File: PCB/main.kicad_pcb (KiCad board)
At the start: 2 copper layers, 21 parts, among them SW1 SPST, U1 MCP2558FD, U2 MCP2558FD, U3 STM32G0B1, Y1 40M

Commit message: Further develop board
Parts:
- added C10: 100u, Capacitor_Tantalum_SMD:CP_EIA-3528-15_AVX-H, F.Cu at (37.7, 48.5)
- added C11: 1u, Capacitor_SMD:C_0805_2012Metric, F.Cu at (32.5, 46.5)
- added C12: 1u, Capacitor_SMD:C_0805_2012Metric, F.Cu at (32.5, 49.5)
- added C13: 100n, Capacitor_SMD:C_0402_1005Metric, F.Cu at (45.7, 37.0)
- added C14: 100n, Capacitor_SMD:C_0402_1005Metric, F.Cu at (45.7, 39.0)
- added C15: 100n, Capacitor_SMD:C_0402_1005Metric, F.Cu at (45.7, 41.0)
- added C7: 100n, Capacitor_SMD:C_0603_1608Metric, F.Cu at (14.7, 48.8)
- added C8: 330u, Capacitor_SMD:CP_Elec_10x10, F.Cu at (37.5, 36.1)
- added C9: 100u, Capacitor_Tantalum_SMD:CP_EIA-3528-15_AVX-H, F.Cu at (37.7, 44.2)
- added D1: SS36, Diode_SMD:D_SMC, F.Cu at (7.28, 46.4)
- added J1: S20B-PADSS-1, libdb:CMP-0012, F.Cu at (15.0, 8.51)
- added J2: S20B-PADSS-1, libdb:CMP-0012, F.Cu at (30.3, 8.51)
- added J4: SWD, libdb:CMP-0022, F.Cu at (21.8, 32.5)
- added L1: 33u, Inductor_SMD:L_1210_3225Metric, F.Cu at (46.5, 11.4)
- added U4: LM2596-5.0, Package_TO_SOT_SMD:TO-263-5_TabPin3, F.Cu at (12.5, 36.3)
- added U5: XC6206P33, libdb:CMP-0019, F.Cu at (46.2, 7.11)
- C1: value 15p -> 100n; footprint Capacitor_SMD:C_0402_1005Metric -> Capacitor_SMD:C_0603_1608Metric
- C2: value 15p -> 4.7u; footprint Capacitor_SMD:C_0402_1005Metric -> Capacitor_SMD:C_0805_2012Metric
- C4: value 100n -> 15p; footprint Capacitor_SMD:C_0603_1608Metric -> Capacitor_SMD:C_0402_1005Metric
- C5: value 4.7u -> 15p; footprint Capacitor_SMD:C_0805_2012Metric -> Capacitor_SMD:C_0402_1005Metric
- C6: footprint Capacitor_SMD:C_0603_1608Metric -> Capacitor_SMD:C_0402_1005Metric
- R10: value 10k -> 0
- R2: value 120 -> 0; footprint Resistor_SMD:R_1206_3216Metric -> Resistor_SMD:R_0402_1005Metric
- R3: value 0 -> 120; footprint Resistor_SMD:R_0402_1005Metric -> Resistor_SMD:R_1206_3216Metric
- R4: value 0 -> 10k
- U2: value MCP2558FD -> STM32G0B1; footprint Package_SO:SOIC-8_3.9x4.9mm_P1.27mm -> Package_QFP:LQFP-48_7x7mm_P0.5mm
- U3: value STM32G0B1 -> MCP2558FD; footprint Package_QFP:LQFP-48_7x7mm_P0.5mm -> Package_SO:SOIC-8_3.9x4.9mm_P1.27mm
- Y1: footprint Crystal:Crystal_SMD_2016-4Pin_2.0x1.6mm -> libdb:CMP-0004
- moved Y1 31.9 mm to (45.6, 15.4)
- moved R2 31.6 mm to (33.8, 5.88)
- moved SW1 30.6 mm to (24.5, 45.7)
- moved R3 28.6 mm to (43.5, 46.9)
- moved C3 26.6 mm to (14.7, 46.2)
- moved U1 22.8 mm to (39.4, 8.11)
- moved C5 20.6 mm to (45.7, 33.1)
- moved U2 19.0 mm to (40.9, 23.5)
- moved R10 18.3 mm to (33.8, 19.8)
- moved R9 18.3 mm to (33.8, 17.8)
- moved C1 17.3 mm to (14.7, 43.7)
- moved R8 17.0 mm to (33.8, 15.8)
- moved R4 17.0 mm to (33.8, 7.87)
- moved R5 17.0 mm to (33.8, 9.86)
- moved R6 17.0 mm to (33.8, 11.8)
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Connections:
- C1 pad 2: Net-(U3-PF0) -> Net-(U2-VREF+)
- C2 pad 2: Net-(U3-PF1) -> Net-(U2-VBAT)
- C3 pad 2: Net-(U3-VBAT) -> Net-(U2-VBAT)
- C4 pad 2: Net-(U3-VREF+) -> Net-(U2-PF0)
- C5 pad 2: Net-(U3-VBAT) -> Net-(U2-PF1)
- C6 pad 1: Net-(U3-PF2) -> Net-(U1-VIO)
- R10 pad 1: /FDCAN2_S -> Net-(U2-PB10)
- R10 pad 2: Earth -> /FDCAN2_S
- R2 pad 1: Net-(U1-CANL) -> Net-(U1-RXD)
- R2 pad 2: Net-(U1-CANH) -> /FDCAN1_RX
- R3 pad 1: /FDCAN1_TX -> Net-(U1-CANL)
- R3 pad 2: Net-(U3-PD1) -> Net-(U1-CANH)
- R4 pad 1: Net-(U1-RXD) -> /FDCAN1_S
- R4 pad 2: /FDCAN1_RX -> Earth
- R5 pad 1: Net-(U2-RXD) -> /FDCAN1_TX
- R5 pad 2: /FDCAN2_RX -> Net-(U2-PD1)
- R6 pad 1: Net-(U3-PB1) -> /FDCAN1_S
- R6 pad 2: /FDCAN2_TX -> Net-(U2-PD3)
- R7 pad 1: Net-(U3-PB10) -> Net-(U3-RXD)
- R7 pad 2: /FDCAN2_S -> /FDCAN2_RX
- R8 pad 1: /FDCAN1_S -> Net-(U2-PB1)
- R8 pad 2: Net-(U3-PD3) -> /FDCAN2_TX
- R9 pad 1: /FDCAN1_S -> /FDCAN2_S
- SW1 pad 2: Net-(U3-PF2) -> Net-(U2-PF2)
- U1 pad 3: unconnected-(U1-VDD-Pad3) -> +5V
- U1 pad 5: unconnected-(U1-VIO-Pad5) -> Net-(U1-VIO)
- U2 pad 1: /FDCAN2_TX -> unconnected-(U2-PC13-Pad1)
- U2 pad 2: Earth -> unconnected-(U2-PC14-Pad2)
- U2 pad 4: Net-(U2-RXD) -> Net-(U2-VBAT)
- U2 pad 5: unconnected-(U2-VIO-Pad5) -> Net-(U2-VREF+)
- U2 pad 6: unconnected-(U2-CANL-Pad6) -> Net-(U2-VBAT)
- U2 pad 7: unconnected-(U2-CANH-Pad7) -> Earth
- U2 pad 8: /FDCAN2_S -> Net-(U2-PF0)
- U3 pad 1: unconnected-(U3-PC13-Pad1) -> /FDCAN2_TX
- U3 pad 2: unconnected-(U3-PC14-Pad2) -> Earth
- U3 pad 3: unconnected-(U3-PC15-Pad3) -> +5V
- U3 pad 4: Net-(U3-VBAT) -> Net-(U3-RXD)
- U3 pad 5: Net-(U3-VREF+) -> Net-(U3-VIO)
- U3 pad 6: Net-(U3-VBAT) -> unconnected-(U3-CANL-Pad6)
- U3 pad 7: Earth -> unconnected-(U3-CANH-Pad7)
- U3 pad 8: Net-(U3-PF0) -> /FDCAN2_S
- Y1 pad 1: Net-(U3-PF0) -> Net-(U2-PF0)
- Y1 pad 3: Net-(U3-PF1) -> Net-(U2-PF1)

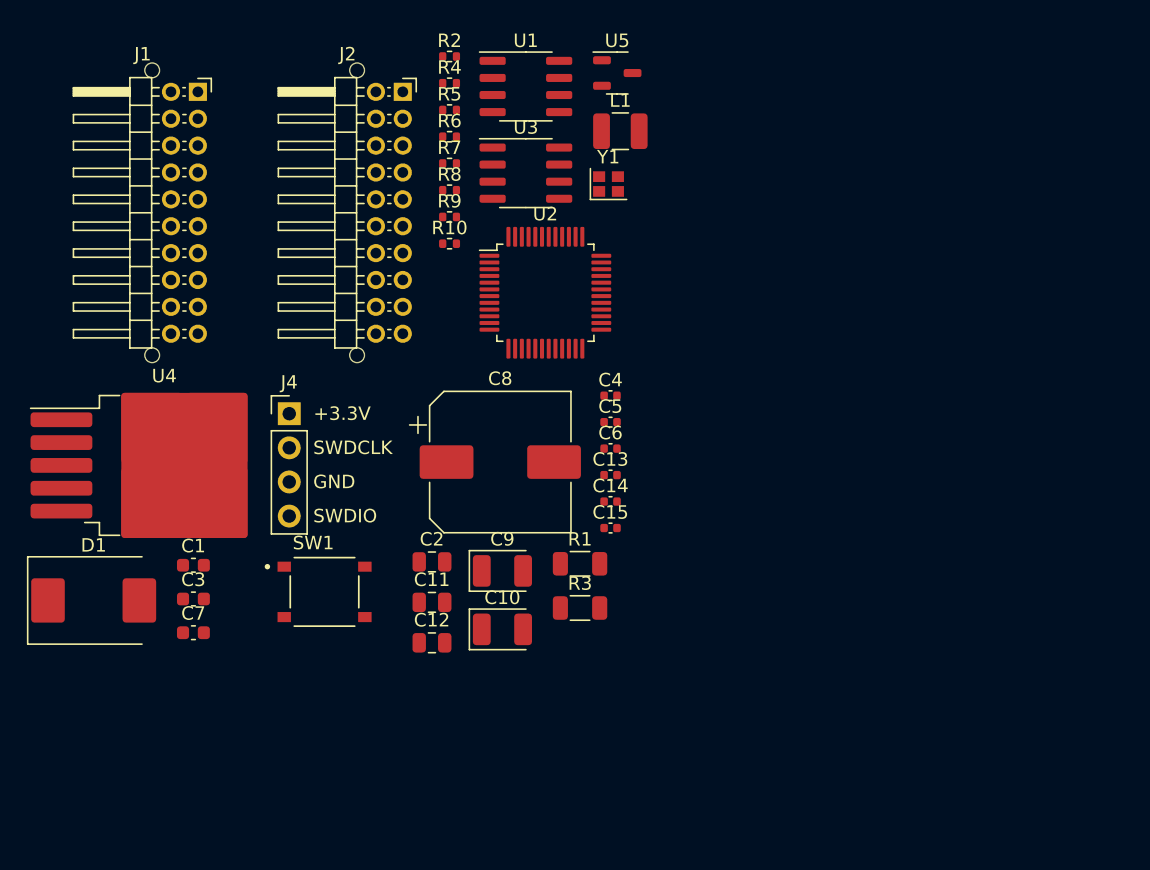
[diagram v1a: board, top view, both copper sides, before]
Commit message: Finish schematic
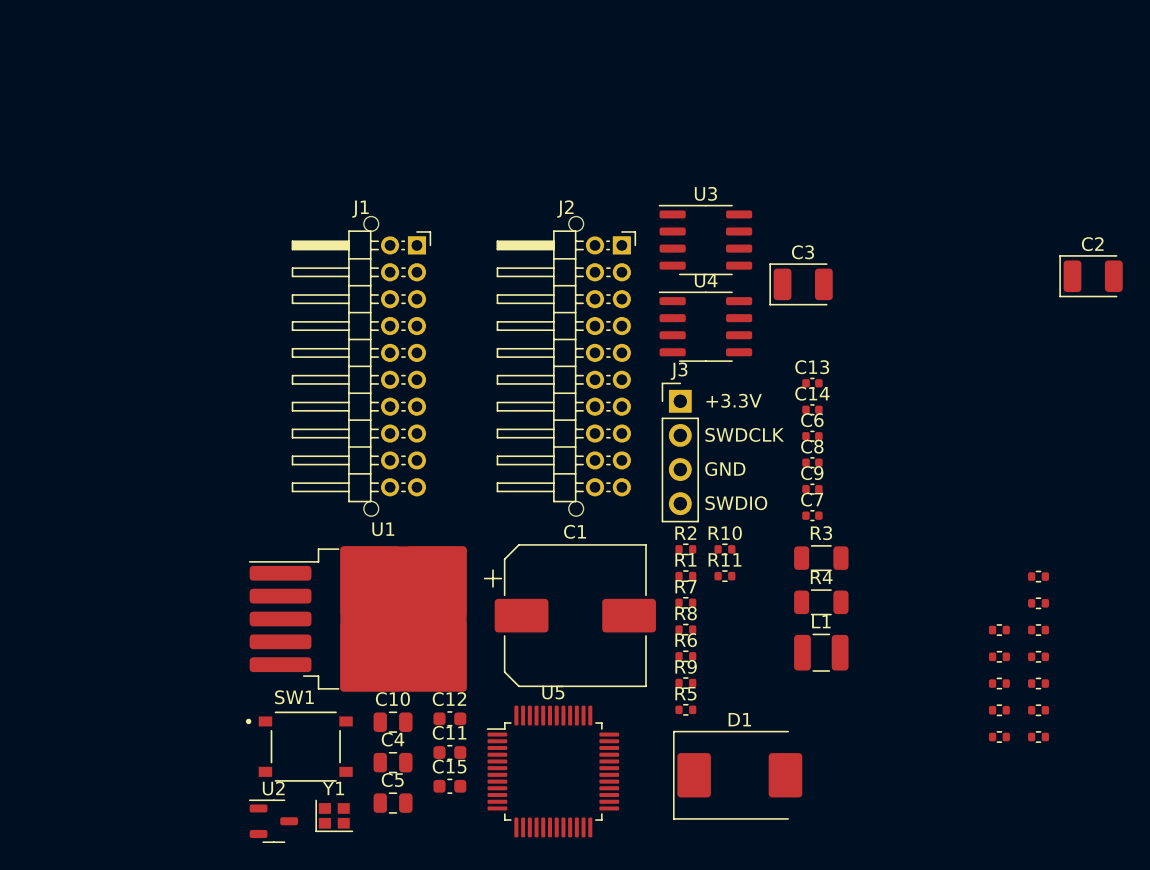
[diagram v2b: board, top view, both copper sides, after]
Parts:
- removed J4: SWD, libdb:CMP-0022
- added J3: SWD, libdb:CMP-0022, F.Cu at (50.9, 31.5)
- added R11: 100, Resistor_SMD:R_0402_1005Metric, F.Cu at (54.3, 44.5)
- added R12: 0, Resistor_SMD:R_0402_1005Metric, F.Cu at (74.7, 48.6)
- added R13: 0, Resistor_SMD:R_0402_1005Metric, F.Cu at (74.7, 50.5)
- added R14: 0, Resistor_SMD:R_0402_1005Metric, F.Cu at (74.7, 52.5)
- added R15: 0, Resistor_SMD:R_0402_1005Metric, F.Cu at (74.7, 54.5)
- added R16: 0, Resistor_SMD:R_0402_1005Metric, F.Cu at (74.7, 56.5)
- added R17: 0, Resistor_SMD:R_0402_1005Metric, F.Cu at (77.6, 44.6)
- added R18: 0, Resistor_SMD:R_0402_1005Metric, F.Cu at (77.6, 46.6)
- added R19: 0, Resistor_SMD:R_0402_1005Metric, F.Cu at (77.6, 48.6)
- added R20: 0, Resistor_SMD:R_0402_1005Metric, F.Cu at (77.6, 50.5)
- added R21: 0, Resistor_SMD:R_0402_1005Metric, F.Cu at (77.6, 52.5)
- added R22: 0, Resistor_SMD:R_0402_1005Metric, F.Cu at (77.6, 54.5)
- added R23: 0, Resistor_SMD:R_0402_1005Metric, F.Cu at (77.6, 56.5)
- C1: value 100n -> 330u; footprint Capacitor_SMD:C_0603_1608Metric -> Capacitor_SMD:CP_Elec_10x10
- C10: value 100u -> 4.7u; footprint Capacitor_Tantalum_SMD:CP_EIA-3528-15_AVX-H -> Capacitor_SMD:C_0805_2012Metric
- C11, C12: value 1u -> 100n; footprint Capacitor_SMD:C_0805_2012Metric -> Capacitor_SMD:C_0603_1608Metric
- C13, C14: value 100n -> 15p
- C15: footprint Capacitor_SMD:C_0402_1005Metric -> Capacitor_SMD:C_0603_1608Metric
- C2: value 4.7u -> 100u; footprint Capacitor_SMD:C_0805_2012Metric -> Capacitor_Tantalum_SMD:CP_EIA-3528-15_AVX-H
- C3: value 100n -> 100u; footprint Capacitor_SMD:C_0603_1608Metric -> Capacitor_Tantalum_SMD:CP_EIA-3528-15_AVX-H
- C4, C5: value 15p -> 1u; footprint Capacitor_SMD:C_0402_1005Metric -> Capacitor_SMD:C_0805_2012Metric
- C7: footprint Capacitor_SMD:C_0603_1608Metric -> Capacitor_SMD:C_0402_1005Metric
- C8: value 330u -> 100n; footprint Capacitor_SMD:CP_Elec_10x10 -> Capacitor_SMD:C_0402_1005Metric
- C9: value 100u -> 100n; footprint Capacitor_Tantalum_SMD:CP_EIA-3528-15_AVX-H -> Capacitor_SMD:C_0402_1005Metric
- R1: value 120 -> 10k; footprint Resistor_SMD:R_1206_3216Metric -> Resistor_SMD:R_0402_1005Metric
- R4: value 10k -> 120; footprint Resistor_SMD:R_0402_1005Metric -> Resistor_SMD:R_1206_3216Metric
- R5: value 0 -> 10k
- R9: value 10k -> 0
- U1: value MCP2558FD -> LM2596-5.0; footprint Package_SO:SOIC-8_3.9x4.9mm_P1.27mm -> Package_TO_SOT_SMD:TO-263-5_TabPin3
- U2: value STM32G0B1 -> XC6206P33; footprint Package_QFP:LQFP-48_7x7mm_P0.5mm -> libdb:CMP-0019
- U4: value LM2596-5.0 -> MCP2558FD; footprint Package_TO_SOT_SMD:TO-263-5_TabPin3 -> Package_SO:SOIC-8_3.9x4.9mm_P1.27mm
- U5: value XC6206P33 -> STM32G0B1; footprint libdb:CMP-0019 -> Package_QFP:LQFP-48_7x7mm_P0.5mm
- moved C2 53.6 mm to (81.7, 22.2)
- moved U5 52.2 mm to (41.5, 59.1)
- moved Y1 51.3 mm to (25.2, 62.4)
- moved C3 51.1 mm to (60.1, 22.8)
- moved D1 49.8 mm to (55.4, 59.4)
- moved R5 48.0 mm to (51.4, 54.5)
- moved R4 47.5 mm to (61.4, 46.5)
- moved C7 46.9 mm to (60.8, 40.0)
- moved U2 44.2 mm to (20.7, 62.8)
- moved R6 42.5 mm to (51.4, 50.5)
- moved U4 41.6 mm to (52.8, 26.0)
- moved L1 41.6 mm to (61.4, 50.2)
- moved U1 41.0 mm to (28.8, 47.7)
- moved R2 40.7 mm to (51.4, 42.6)
- moved R9 38.9 mm to (51.4, 52.5)
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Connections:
- C1 pad 1: Earth -> +BATT
- C1 pad 2: Net-(U2-VREF+) -> Earth
- C10 pad 1: +5V -> +3.3V
- C11 pad 1: +5V -> +3.3V
- C12 pad 1: +3.3V -> Earth
- C12 pad 2: Earth -> Net-(U5-VREF+)
- C13 pad 1: Net-(U3-VIO) -> Earth
- C13 pad 2: Earth -> Net-(U5-PF0)
- C14 pad 1: +5V -> Earth
- C14 pad 2: Earth -> Net-(U5-PF1)
- C15 pad 1: +5V -> Net-(U5-PF2)
- C2 pad 1: Earth -> +5V
- C2 pad 2: Net-(U2-VBAT) -> Earth
- C3 pad 1: Earth -> +5V
- C3 pad 2: Net-(U2-VBAT) -> Earth
- C4 pad 1: Earth -> +5V
- C4 pad 2: Net-(U2-PF0) -> Earth
- C5 pad 1: Earth -> +3.3V
- C5 pad 2: Net-(U2-PF1) -> Earth
- C6 pad 1: Net-(U1-VIO) -> +3.3V
- C7 pad 1: Net-(U2-PF2) -> +5V
- C8 pad 1: +BATT -> +3.3V
- J1 pad 17: /JST_17_CAN -> /JST_17_CAN1H
- J1 pad 18: /JST_18_CAN -> /JST_18_CAN2H_NC
- J1 pad 6: /JST_06_CAN -> /JST_06_CAN1L
- J1 pad 7: /JST_07_CAN -> /JST_07_CAN2L_NC
- J2 pad 13: /JST_18_CAN -> /CAN2H_NC
- J2 pad 14: /JST_17_CAN -> /CAN1H
- J2 pad 4: /JST_07_CAN -> /CAN2L_NC
- J2 pad 5: /JST_06_CAN -> /CAN1L
- R1 pad 1: Net-(U1-CANL) -> /FDCAN1_S
- R1 pad 2: Net-(U1-CANH) -> Earth
- R10 pad 1: Net-(U2-PB10) -> Net-(U5-PB10)
- R2 pad 1: Net-(U1-RXD) -> Net-(U3-RXD)
- R3 pad 1: Net-(U1-CANL) -> /Relay_OUT_CANL
- R3 pad 2: Net-(U1-CANH) -> /Relay_OUT_CANH
- R4 pad 1: /FDCAN1_S -> /Relay_OUT_CANL
- R4 pad 2: Earth -> /Relay_OUT_CANH
- R5 pad 1: /FDCAN1_TX -> /FDCAN2_S
- R5 pad 2: Net-(U2-PD1) -> Earth
- R6 pad 1: /FDCAN1_S -> Net-(U4-RXD)
- R6 pad 2: Net-(U2-PD3) -> /FDCAN2_RX
- R7 pad 1: Net-(U3-RXD) -> /FDCAN1_TX
- R7 pad 2: /FDCAN2_RX -> Net-(U5-PD1)
- R8 pad 1: Net-(U2-PB1) -> /FDCAN1_S
- R8 pad 2: /FDCAN2_TX -> Net-(U5-PD3)
- R9 pad 1: /FDCAN2_S -> Net-(U5-PB1)
- R9 pad 2: Earth -> /FDCAN2_TX
- SW1 pad 2: Net-(U2-PF2) -> Net-(U5-PF2)
- U1 pad 1: /FDCAN1_TX -> +BATT
- U1 pad 2: Earth -> Net-(D1-K)
- U1 pad 3: +5V -> Earth
- U1 pad 4: Net-(U1-RXD) -> +5V
- U1 pad 5: Net-(U1-VIO) -> Earth
- U2 pad 1: unconnected-(U2-PC13-Pad1) -> Earth
- U2 pad 2: unconnected-(U2-PC14-Pad2) -> +3.3V
- U2 pad 3: unconnected-(U2-PC15-Pad3) -> +5V
- U3 pad 1: /FDCAN2_TX -> /FDCAN1_TX
- U3 pad 5: Net-(U3-VIO) -> +3.3V
- U3 pad 6: unconnected-(U3-CANL-Pad6) -> /Relay_OUT_CANL
- U3 pad 7: unconnected-(U3-CANH-Pad7) -> /Relay_OUT_CANH
- U3 pad 8: /FDCAN2_S -> /FDCAN1_S
- U4 pad 1: +BATT -> /FDCAN2_TX
- U4 pad 2: Net-(D1-K) -> Earth
- U4 pad 3: Earth -> +5V
- U4 pad 4: +5V -> Net-(U4-RXD)
- U4 pad 5: Earth -> +3.3V
- U5 pad 1: Earth -> unconnected-(U5-PC13-Pad1)
- U5 pad 2: +3.3V -> unconnected-(U5-PC14-Pad2)
- U5 pad 3: +5V -> unconnected-(U5-PC15-Pad3)
- Y1 pad 1: Net-(U2-PF0) -> Net-(U5-PF0)
- Y1 pad 3: Net-(U2-PF1) -> Net-(U5-PF1)

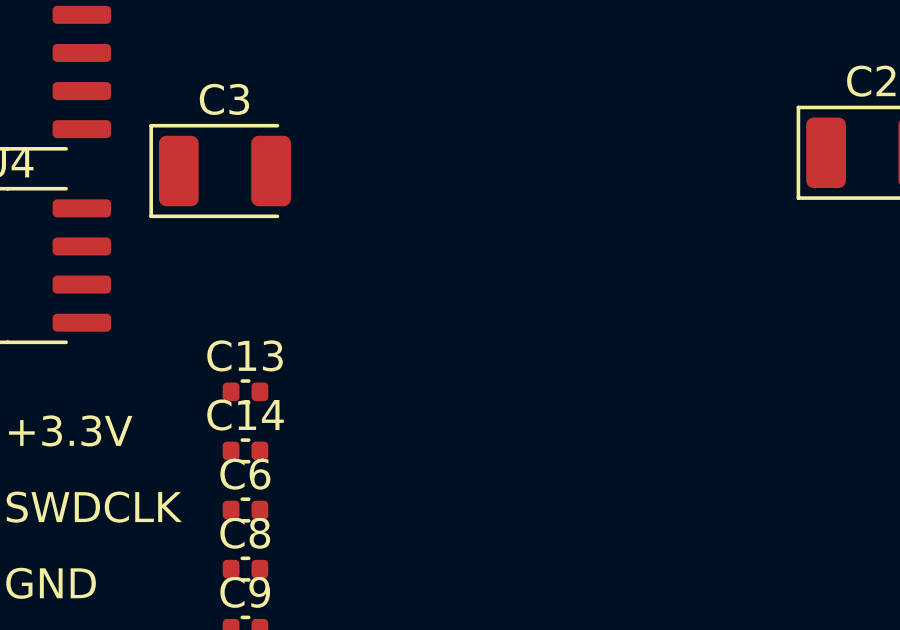
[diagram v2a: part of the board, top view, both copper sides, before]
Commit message: Switch Silent mode on by default
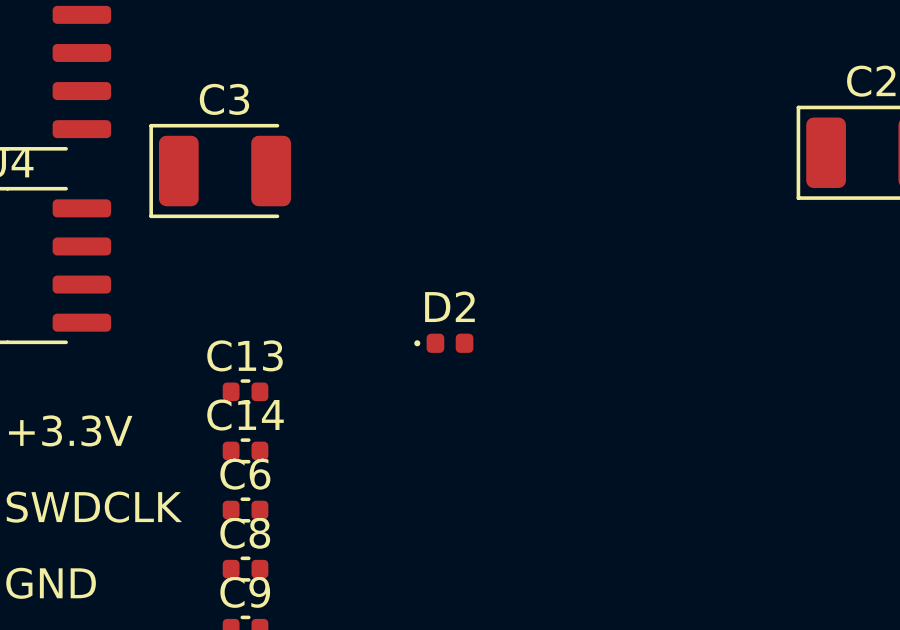
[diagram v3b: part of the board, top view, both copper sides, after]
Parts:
- added D2: LED_B, LED_SMD:LED_0402_1005Metric, F.Cu at (67.6, 28.6)
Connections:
- R1 pad 2: Earth -> +3.3V
- R5 pad 2: Earth -> +3.3V
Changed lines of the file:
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@@
       (net 12 "/FDCAN2_S") (pintype "passive"))
     (pad "2" smd roundrect (at 0.51 0) (size 0.54 0.64) (layers "F.Cu" "F.Paste" "F.Mask") (roundrect_rratio 0.25)
-      (net 1 "Earth") (pintype "passive"))
+      (net 11 "+3.3V") (pintype "passive"))
     (model "${KICAD6_3DMODEL_DIR}/Resistor_SMD.3dshapes/R_0402_1005Metric.wrl"
       (offset (xyz 0 0 0))
@@
       (net 13 "/FDCAN1_S") (pintype "passive"))
     (pad "2" smd roundrect (at 0.51 0) (size 0.54 0.64) (layers "F.Cu" "F.Paste" "F.Mask") (roundrect_rratio 0.25)
-      (net 1 "Earth") (pintype "passive"))
+      (net 11 "+3.3V") (pintype "passive"))
     (model "${KICAD6_3DMODEL_DIR}/Resistor_SMD.3dshapes/R_0402_1005Metric.wrl"
       (offset (xyz 0 0 0))
@@
       (offset (xyz 0 0 0))
       (scale (xyz 1 1 1))
+      (rotate (xyz 0 0 0))
+    )
+  )
+  (footprint "LED_SMD:LED_0402_1005Metric" (layer "F.Cu")
+    (at 67.587 28.575)
+    (descr "LED SMD 0402 (1005 Metric), square (rectangular) end terminal, IPC_7351 nominal, (Body size source: http://www.tortai-tech.com/upload/download/2011102023233369053.pdf), generated with kicad-footprint-generator")
+    (tags "LED")
+    (property "Case/Package Size" "0603")
+    (property "Colour" "Blue")
+    (property "Forward Voltage" "2.8V")
+    (property "LCSC" "LCSC: C72041")
+    (property "MPN" "19-217/BHC-ZL1M2RY/3T")
+    (property "Manufacturer" "Everlight Electronics")
+    (property "Maximum DC Current" "25m")
+    (property "Reverse Current" "50u")
+    (property "Sheetfile" "main.kicad_sch")
+    (property "Sheetname" "")
+    (property "ki_description" "Blue LED Indication - Discrete 2.8V 0603 (1608 Metric)")
+    (property "ki_keywords" "LED diode light-emitting-diode")
+    (attr smd)
+    (fp_text reference "D2" (at 0 -1.17) (layer "F.SilkS")
+        (effects (font (size 1 1) (thickness 0.15)))
+    )
+    (fp_text value "LED_B" (at 0 1.17) (layer "F.Fab")
+        (effects (font (size 1 1) (thickness 0.15)))
+    )
+    (fp_text user "${REFERENCE}" (at 0 0) (layer "F.Fab")
+        (effects (font (size 0.25 0.25) (thickness 0.04)))
+    )
+    (fp_circle (center -1.09 0) (end -1.04 0)
+      (stroke (width 0.1) (type solid)) (fill none) (layer "F.SilkS"))
+    (fp_line (start -0.93 -0.47) (end 0.93 -0.47)
+      (stroke (width 0.05) (type solid)) (layer "F.CrtYd"))
+    (fp_line (start -0.93 0.47) (end -0.93 -0.47)
+      (stroke (width 0.05) (type solid)) (layer "F.CrtYd"))
+    (fp_line (start 0.93 -0.47) (end 0.93 0.47)
+      (stroke (width 0.05) (type solid)) (layer "F.CrtYd"))
+    (fp_line (start 0.93 0.47) (end -0.93 0.47)
+      (stroke (width 0.05) (type solid)) (layer "F.CrtYd"))
+    (fp_line (start -0.5 -0.25) (end 0.5 -0.25)
+      (stroke (width 0.1) (type solid)) (layer "F.Fab"))
+    (fp_line (start -0.5 0.25) (end -0.5 -0.25)
+      (stroke (width 0.1) (type solid)) (layer "F.Fab"))
+    (fp_line (start -0.4 0.25) (end -0.4 -0.25)
+      (stroke (width 0.1) (type solid)) (layer "F.Fab"))
+    (fp_line (start -0.3 0.25) (end -0.3 -0.25)
+      (stroke (width 0.1) (type solid)) (layer "F.Fab"))
+    (fp_line (start 0.5 -0.25) (end 0.5 0.25)
+      (stroke (width 0.1) (type solid)) (layer "F.Fab"))
+    (fp_line (start 0.5 0.25) (end -0.5 0.25)
+      (stroke (width 0.1) (type solid)) (layer "F.Fab"))
+    (pad "1" smd roundrect (at -0.485 0) (size 0.59 0.64) (layers "F.Cu" "F.Paste" "F.Mask") (roundrect_rratio 0.25)
+      (net 1 "Earth") (pinfunction "K") (pintype "passive"))
+    (pad "2" smd roundrect (at 0.485 0) (size 0.59 0.64) (layers "F.Cu" "F.Paste" "F.Mask") (roundrect_rratio 0.25)
+      (net 51 "Net-(D2-A)") (pinfunction "A") (pintype "passive"))
+    (model "${KICAD6_3DMODEL_DIR}/LED_SMD.3dshapes/LED_0402_1005Metric.wrl"
+      (offset (xyz 0 0 0))
+      (scale (xyz 1 1 1))
